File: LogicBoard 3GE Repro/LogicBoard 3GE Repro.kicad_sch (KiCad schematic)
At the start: 162 parts, among them IC201 27C512PLCC, IC204 CY62256-70PC, IC206 68A09, IC207 6522, IC208 YM2149, IC301 MC1408, IC302 CD4052B, IC303 LF347, IC304 LF353, IC305 4066, J201 CART, J202 DB9_Male, J203 DB9_Male, J204 Power, J301 Video, J302 Audio, Q301 2N3905, Q302 2N3905, Q303 2N3904, SW201 Reset, U1 ATF16V8Bxx-xxPU, Y201 6MHz

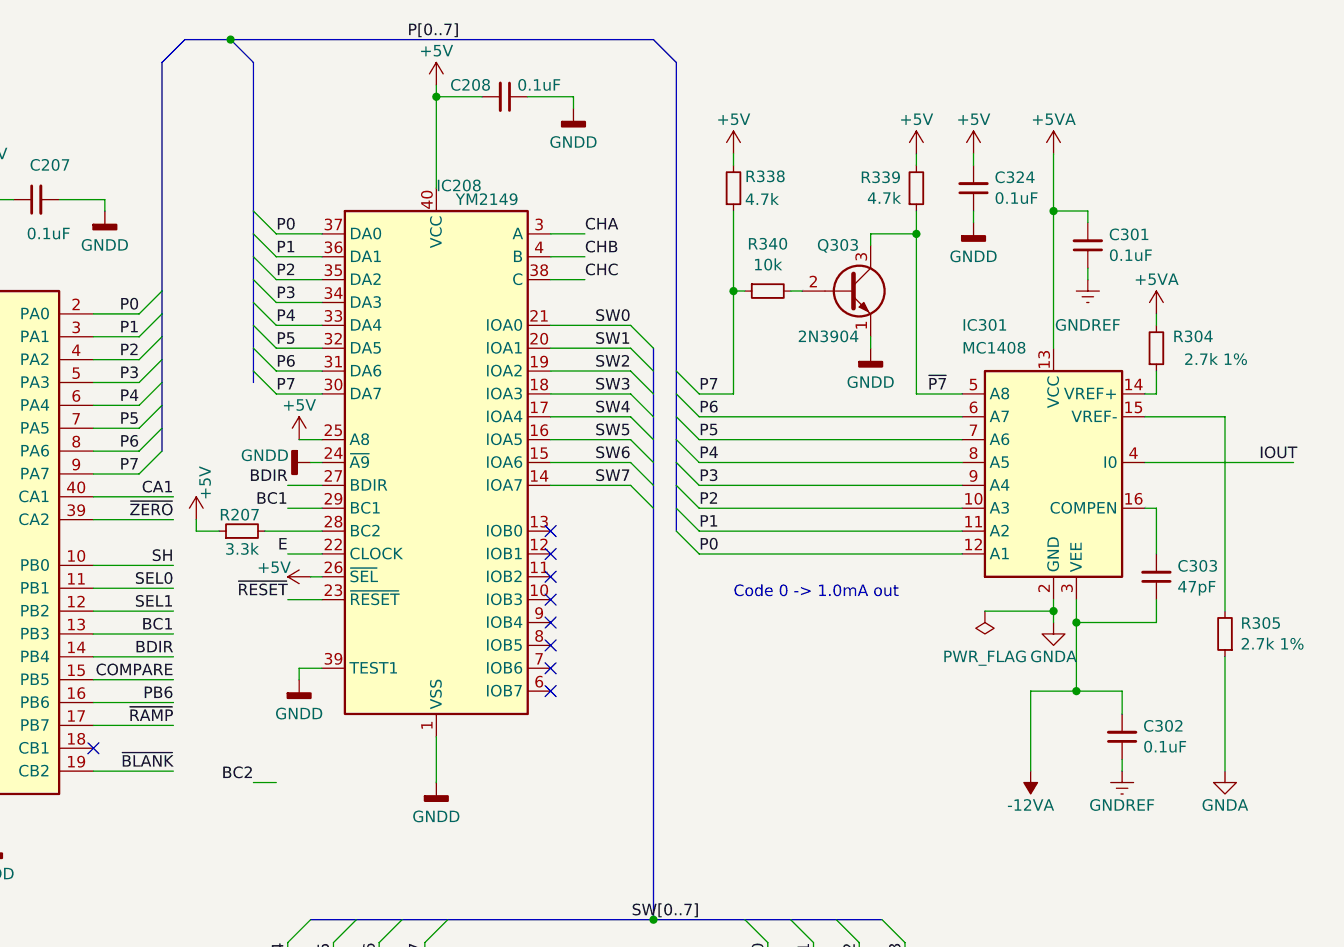
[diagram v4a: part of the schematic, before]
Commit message: Repro: cleanup pass - fix dangling wires (incl. real MC1408 IOUT) + BC2 label
Reconnected IC301 pin4 IOUT (was dangling - real bug), named BC2 net,
removed leftover wire stubs. ERC down to 11 (all intentional/benign).

Co-Authored-By: Claude Opus 4.8 <noreply@anthropic.com>
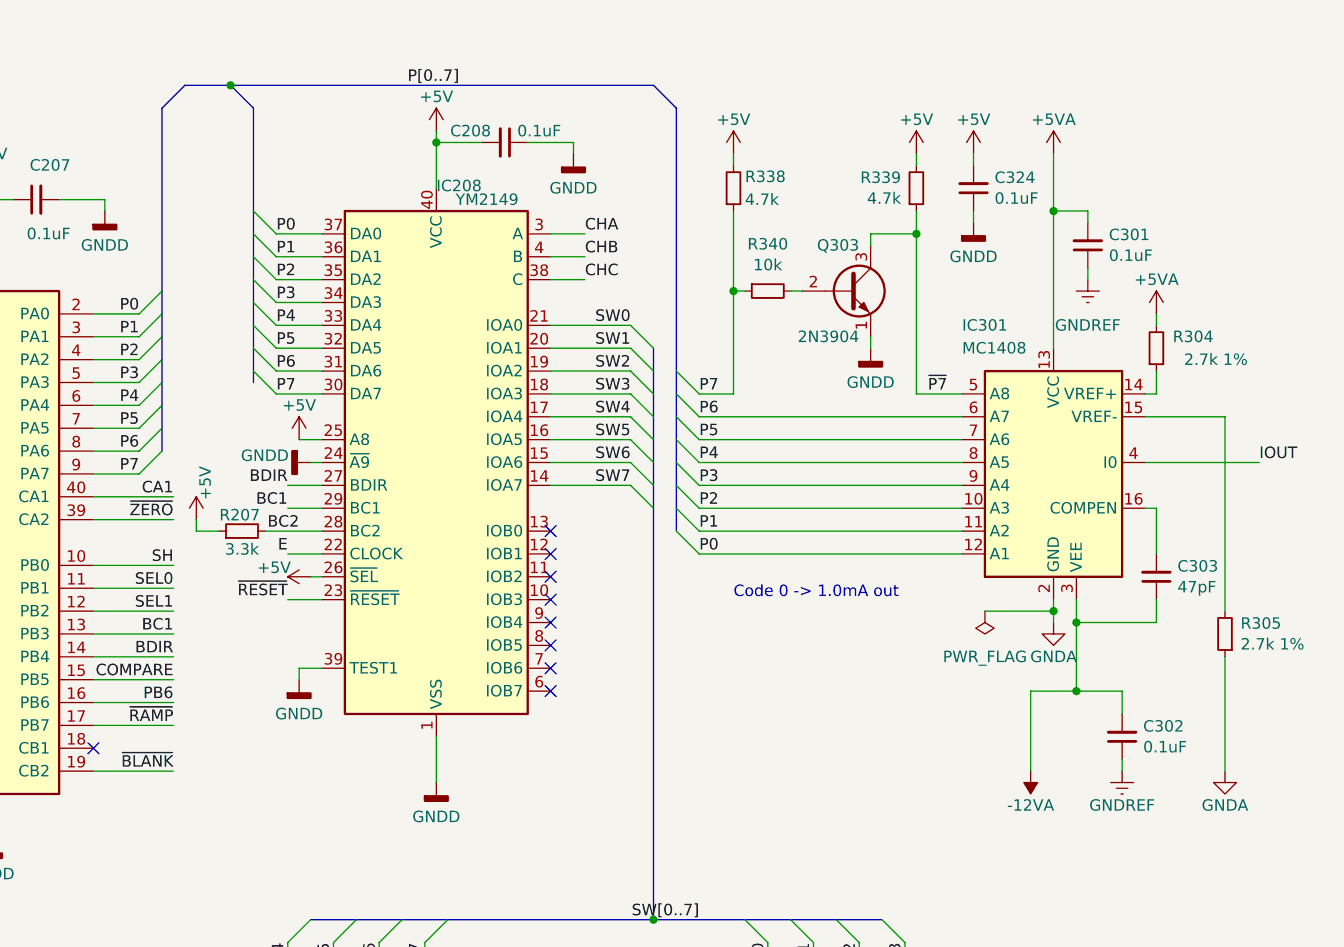
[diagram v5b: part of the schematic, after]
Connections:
- net BC2: now also IC208.28 (BC2), R207.2
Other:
- moved on the sheet: C208
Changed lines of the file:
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@@
 	)
 	(junction
-		(at 280.67 12.7)
+		(at 280.67 17.78)
 		(diameter 0)
 		(color 0 0 0 0)
@@
 	)
 	(junction
-		(at 303.53 19.05)
+		(at 303.53 24.13)
 		(diameter 0)
 		(color 0 0 0 0)
@@
 	(bus
 		(pts
-			(xy 275.59 12.7) (xy 280.67 12.7)
+			(xy 275.59 17.78) (xy 280.67 17.78)
 		)
 		(stroke
@@
 	(wire
 		(pts
-			(xy 283.21 95.25) (xy 285.75 95.25)
-		)
-		(stroke
-			(width 0)
-			(type default)
-		)
-	)
-	(wire
-		(pts
 			(xy 332.74 67.31) (xy 361.95 67.31)
 		)
@@
 	(wire
 		(pts
-			(xy 303.53 17.78) (xy 303.53 29.21)
-		)
-		(stroke
-			(width 0)
-			(type default)
-		)
-	)
-	(wire
-		(pts
 			(xy 212.09 261.62) (xy 212.09 196.85)
 		)
@@
 	(bus
 		(pts
-			(xy 275.59 12.7) (xy 273.05 15.24)
+			(xy 275.59 17.78) (xy 273.05 20.32)
 		)
 		(stroke
@@
 	(bus
 		(pts
-			(xy 280.67 12.7) (xy 327.66 12.7)
+			(xy 280.67 17.78) (xy 327.66 17.78)
 		)
 		(stroke
@@
 		)
 	)
+	(bus
+		(pts
+			(xy 283.21 20.32) (xy 283.21 50.8)
+		)
+		(stroke
+			(width 0)
+			(type default)
+		)
+	)
 	(wire
 		(pts
@@
 	(wire
 		(pts
-			(xy 382.27 59.69) (xy 398.78 59.69)
-		)
-		(stroke
-			(width 0)
-			(type default)
-		)
-	)
-	(wire
-		(pts
 			(xy 95.25 177.8) (xy 92.71 177.8)
 		)
@@
 		)
 	)
-	(bus
-		(pts
-			(xy 283.21 15.24) (xy 283.21 50.8)
-		)
-		(stroke
-			(width 0)
-			(type default)
-		)
-	)
 	(wire
 		(pts
@@
 		)
 	)
+	(bus
+		(pts
+			(xy 273.05 20.32) (xy 273.05 40.64)
+		)
+		(stroke
+			(width 0)
+			(type default)
+		)
+	)
 	(wire
 		(pts
@@
 	(wire
 		(pts
+			(xy 303.53 22.86) (xy 303.53 29.21)
+		)
+		(stroke
+			(width 0)
+			(type default)
+		)
+	)
+	(wire
+		(pts
 			(xy 332.74 52.07) (xy 336.55 52.07)
 		)
@@
 	(bus
 		(pts
+			(xy 330.2 20.32) (xy 330.2 49.53)
+		)
+		(stroke
+			(width 0)
+			(type default)
+		)
+	)
+	(bus
+		(pts
 			(xy 327.66 49.53) (xy 327.66 52.07)
 		)
@@
 	(wire
 		(pts
-			(xy 318.77 19.05) (xy 318.77 20.32)
+			(xy 318.77 24.13) (xy 318.77 25.4)
 		)
 		(stroke
@@
 	(wire
 		(pts
+			(xy 382.27 59.69) (xy 394.97 59.69)
+		)
+		(stroke
+			(width 0)
+			(type default)
+		)
+	)
+	(wire
+		(pts
 			(xy 33.02 53.34) (xy 26.67 53.34)
 		)
@@
 	(bus
 		(pts
-			(xy 327.66 12.7) (xy 330.2 15.24)
+			(xy 327.66 17.78) (xy 330.2 20.32)
 		)
 		(stroke
@@
 	(wire
 		(pts
-			(xy 303.53 19.05) (xy 308.61 19.05)
+			(xy 303.53 24.13) (xy 308.61 24.13)
 		)
 		(stroke
@@
 		)
 	)
-	(bus
-		(pts
-			(xy 330.2 15.24) (xy 330.2 49.53)
-		)
-		(stroke
-			(width 0)
-			(type default)
-		)
-	)
 	(wire
 		(pts
@@
 	(bus
 		(pts
-			(xy 280.67 12.7) (xy 283.21 15.24)
+			(xy 280.67 17.78) (xy 283.21 20.32)
 		)
 		(stroke
@@
 	(wire
 		(pts
-			(xy 313.69 19.05) (xy 318.77 19.05)
+			(xy 313.69 24.13) (xy 318.77 24.13)
 		)
 		(stroke
@@
 		)
 	)
-	(bus
-		(pts
-			(xy 273.05 15.24) (xy 273.05 40.64)
-		)
-		(stroke
-			(width 0)
-			(type default)
-		)
-	)
 	(wire
 		(pts
@@
 		)
 	)
+	(label "BC2"
+		(at 288.29 67.31 180)
+		(effects
+			(font
+				(size 1.27 1.27)
+			)
+			(justify right bottom)
+		)
+	)
 	(label "SW3"
 		(at 325.12 52.07 180)
@@
 	)
 	(label "P[0..7]"
-		(at 306.07 12.7 180)
+		(at 306.07 17.78 180)
 		(effects
 			(font
@@
 		)
 	)
-	(label "BC2"
-		(at 283.21 95.25 180)
-		(effects
-			(font
-				(size 1.27 1.27)
-			)
-			(justify right bottom)
-		)
-	)
 	(label "D5"
 		(at 236.22 88.9 0)
@@
 	(symbol
 		(lib_id "power:GNDD")
-		(at 318.77 20.32 0)
+		(at 318.77 25.4 0)
 		(unit 1)
 		(body_style 1)
@@
 		(dnp no)
 		(property "Reference" "#PWR0178"
-			(at 318.77 26.67 0)
+			(at 318.77 31.75 0)
 			(hide yes)
 			(show_name no)
@@
 		)
 		(property "Value" "GNDD"
-			(at 318.77 24.13 0)
+			(at 318.77 29.21 0)
 			(show_name no)
 			(do_not_autoplace no)
@@
 		)
 		(property "Footprint" ""
-			(at 318.77 20.32 0)
+			(at 318.77 25.4 0)
 			(hide yes)
 			(show_name no)
@@
 		)
 		(property "Datasheet" ""
-			(at 318.77 20.32 0)
+			(at 318.77 25.4 0)
 			(hide yes)
 			(show_name no)
@@
 		)
 		(property "Description" "Power symbol creates a global label with name \"GNDD\" , digital ground"
-			(at 318.77 20.32 0)
+			(at 318.77 25.4 0)
 			(hide yes)
 			(show_name no)
@@
 	(symbol
 		(lib_id "power:+5V")
-		(at 303.53 17.78 0)
+		(at 303.53 22.86 0)
 		(unit 1)
 		(body_style 1)
@@
 		(dnp no)
 		(property "Reference" "#PWR0164"
-			(at 303.53 21.59 0)
+			(at 303.53 26.67 0)
 			(hide yes)
 			(show_name no)
@@
 		)
 		(property "Value" "+5V"
-			(at 303.53 13.97 0)
+			(at 303.53 19.05 0)
 			(show_name no)
 			(do_not_autoplace no)
@@
 		)
 		(property "Footprint" ""
-			(at 303.53 17.78 0)
+			(at 303.53 22.86 0)
 			(hide yes)
 			(show_name no)
@@
 		)
 		(property "Datasheet" ""
-			(at 303.53 17.78 0)
+			(at 303.53 22.86 0)
 			(hide yes)
 			(show_name no)
@@
 		)
 		(property "Description" "Power symbol creates a global label with name \"+5V\""
-			(at 303.53 17.78 0)
+			(at 303.53 22.86 0)
 			(hide yes)
 			(show_name no)
@@
 	(symbol
 		(lib_id "Device:C_Small")
-		(at 311.15 19.05 270)
+		(at 311.15 24.13 270)
 		(unit 1)
 		(body_style 1)
@@
 		(dnp no)
 		(property "Reference" "C208"
-			(at 307.34 17.78 90)
+			(at 307.34 22.86 90)
 			(show_name no)
 			(do_not_autoplace no)
@@
 		)
 		(property "Value" "0.1uF"
-			(at 314.96 17.78 90)
+			(at 314.96 22.86 90)
 			(show_name no)
 			(do_not_autoplace no)
@@
 		)
 		(property "Footprint" "Capacitor_THT:C_Disc_D5.0mm_W2.5mm_P5.00mm"
-			(at 311.15 19.05 0)
+			(at 311.15 24.13 0)
 			(hide yes)
 			(show_name no)
@@
 		)
 		(property "Datasheet" ""
-			(at 311.15 19.05 0)
+			(at 311.15 24.13 0)
 			(hide yes)
 			(show_name no)
@@
 		)
 		(property "Description" "Unpolarized capacitor, small symbol"
-			(at 311.15 19.05 0)
+			(at 311.15 24.13 0)
 			(hide yes)
 			(show_name no)
@@
 		)
 		(property "Mouser" "581-SR215C104k"
-			(at 280.67 -210.82 0)
+			(at 280.67 -205.74 0)
 			(hide yes)
 			(show_name no)

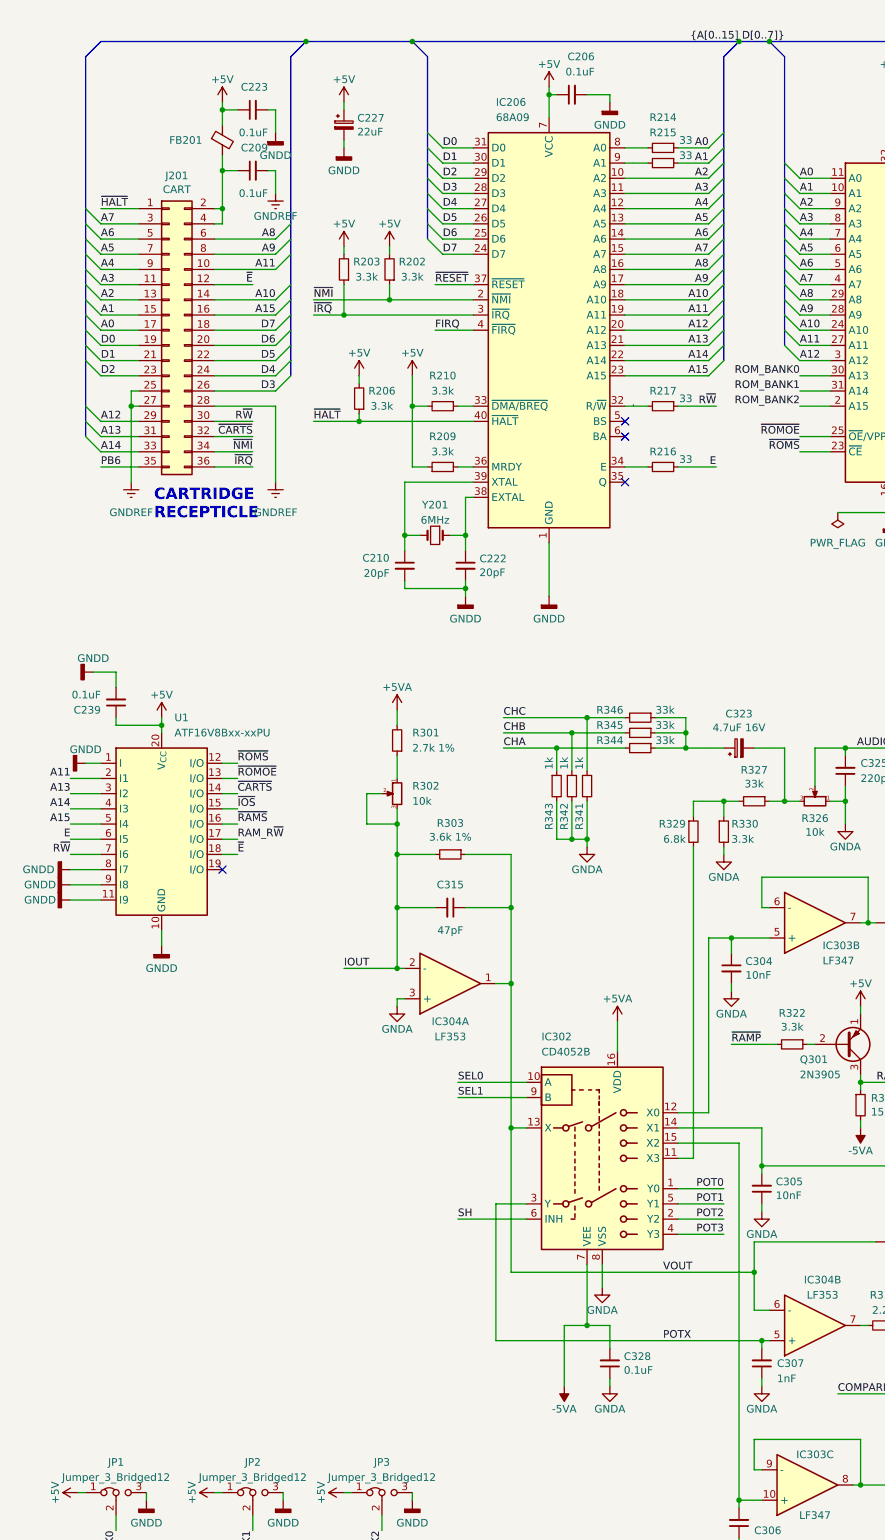
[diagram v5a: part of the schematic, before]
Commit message: Repro: CPU substitution - MC6809E + 74HC74/XO32 clock gen (Phase 1 complete)
IC206 swapped to MC6809E (E variant): E/Q now inputs, TSC=GND, removed
crystal Y201 + R209/R210 (MRDY/DMA pull-ups n/a on E variant). Added
OSC1 (6MHz XO32) + IC209 (74HC74 Johnson div-4) generating E + Q clocks.
All 5 substitutions done; VIA stays 6522 symbol (W65C22 PLCC footprint in Phase 2).

Co-Authored-By: Claude Opus 4.8 <noreply@anthropic.com>
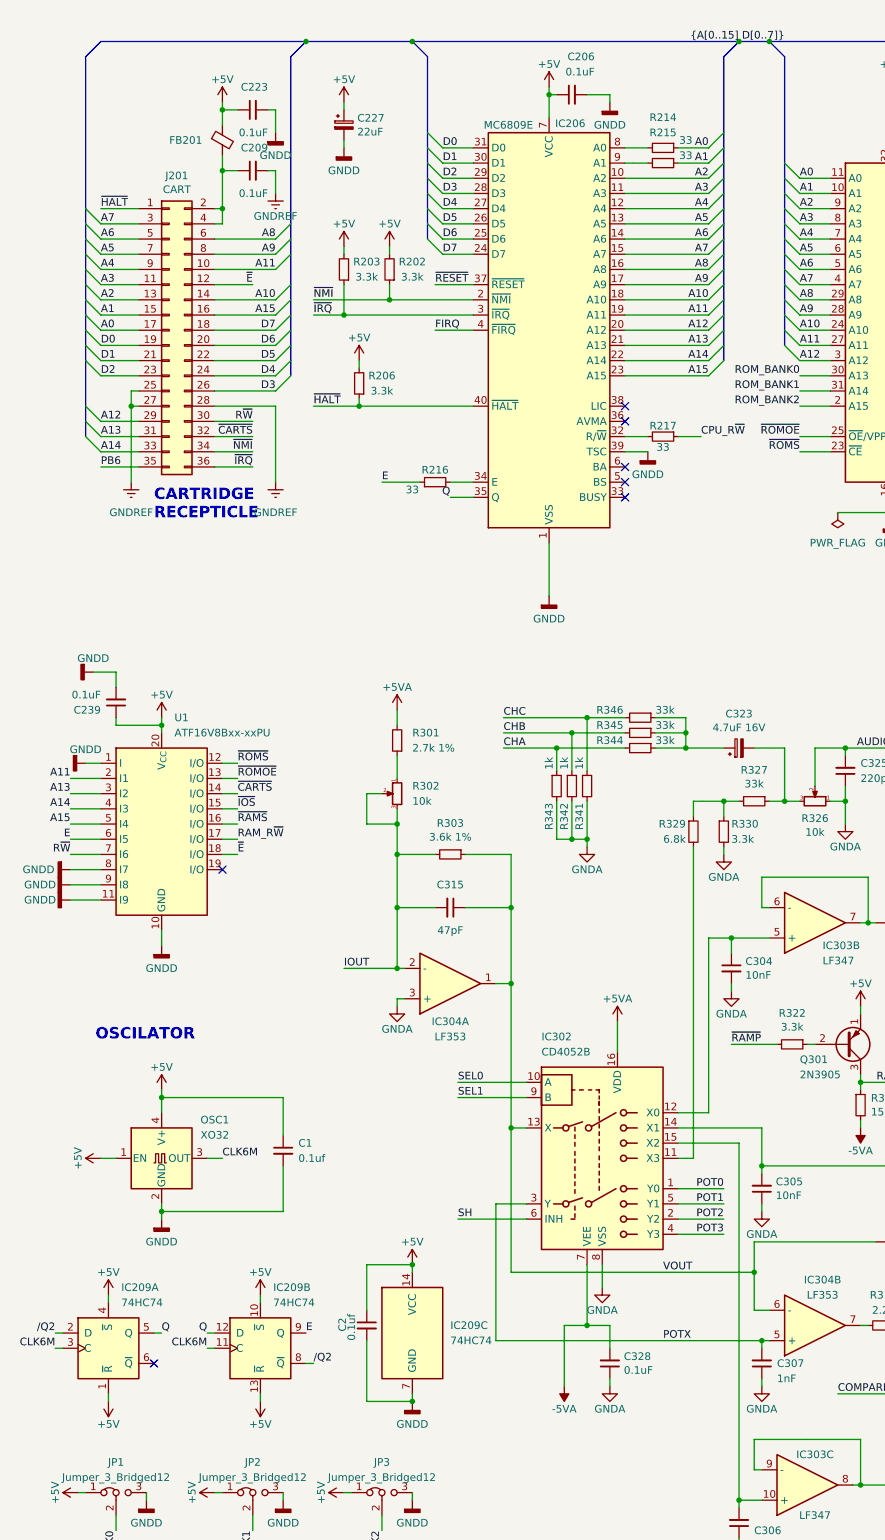
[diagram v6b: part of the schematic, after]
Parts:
- removed C210, C222: 20pF, Capacitor_THT:C_Disc_D5.0mm_W2.5mm_P5.00mm, symbol Device:C_Small
- removed IC206: 68A09, Package_DIP:DIP-40_W15.24mm, symbol Vectrex LogicBoard:MC6809
- removed R209, R210: 3.3k, Vectrex LogicBoard:R_Axial_DIN0207_L6.3mm_D2.5mm_P12.70mm_Horizontal, symbol Device:R_Small
- removed Y201: 6MHz, Vectrex LogicBoard:Crystal_HC49-U_Horizontal_1EP_style3, symbol Device:Crystal_Small
- added C1, C2: 0.1uf, symbol Device:C_Small
- added IC206: MC6809E, Package_DIP:DIP-40_W15.24mm, symbol CPU_NXP_6800:MC6809E
- added IC209: 74HC74, symbol 74xx:74HC74
- added OSC1: XO32, Oscillator:Oscillator_SMD_EuroQuartz_XO32-4Pin_3.2x2.5mm, symbol Oscillator:XO32
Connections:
- net +5V: now also C1.1, C2.1, IC206.7 (VCC), IC209.1 (~{R}), IC209.10 (~{S}), IC209.13 (~{R}), IC209.14 (VCC), IC209.4 (~{S}), OSC1.1 (EN), OSC1.4 (V+)
- net A10: now also IC206.18 (A10)
- net A11: now also IC206.19 (A11)
- net A12: now also IC206.20 (A12)
- net A13: now also IC206.21 (A13)
- net A14: now also IC206.22 (A14)
- net A15: now also IC206.23 (A15)
- net A2: now also IC206.10 (A2)
- net A3: now also IC206.11 (A3)
- net A4: now also IC206.12 (A4)
- net A5: now also IC206.13 (A5)
- net A6: now also IC206.14 (A6)
- net A7: now also IC206.15 (A7)
- net A8: now also IC206.16 (A8)
- net A9: now also IC206.17 (A9)
- net CPU_A0: now also IC206.8 (A0)
- net CPU_A1: now also IC206.9 (A1)
- net CPU_E: now also IC206.34 (E)
- net CPU_R~{W}: now also R217.1; no longer R217.2
- net D0: now also IC206.31 (D0)
- net D1: now also IC206.30 (D1)
- net D2: now also IC206.29 (D2)
- net D3: now also IC206.28 (D3)
- net D4: now also IC206.27 (D4)
- net D5: now also IC206.26 (D5)
- net D6: now also IC206.25 (D6)
- net D7: now also IC206.24 (D7)
- net E: now also IC209.9 (Q)
- net FIRQ: now also IC206.4 (~{FIRQ})
- net GNDD: now also C1.2, C2.2, IC206.1 (VSS), IC206.39 (TSC), IC209.7 (GND), OSC1.2 (GND)
- net R~{W}: no longer R217.1
- net ~{HALT}: now also IC206.40 (~{HALT})
- net ~{IRQ}: now also IC206.3 (~{IRQ})
- net ~{NMI}: now also IC206.2 (~{NMI})
- net ~{RESET}: now also IC206.37 (~{RESET})
- new net: IC206.32 (R/~{W}), R217.2
- new net CLK6M: IC209.11 (C), IC209.3 (C), OSC1.3 (OUT)
- new net Q: IC206.35 (Q), IC209.12 (D), IC209.5 (Q)
- new net /Q2: IC209.2 (D), IC209.8 (~{Q})
- no-connect marks 14 -> 17
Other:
- note added: "OSCILATOR"
- moved on the sheet: R206, R216, R217
